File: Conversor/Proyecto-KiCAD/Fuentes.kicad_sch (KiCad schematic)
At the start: 18 parts, among them J1 Barrel_Jack_Switch, J8 VDDA Header, J9 5V Header, P2 SW_SPDT, P3 SW_SPDT, P5 5V Header, P6 Jumper 2, U5 LM7805_TO252, U6 THB3-1211, U7 LP2985-3.3

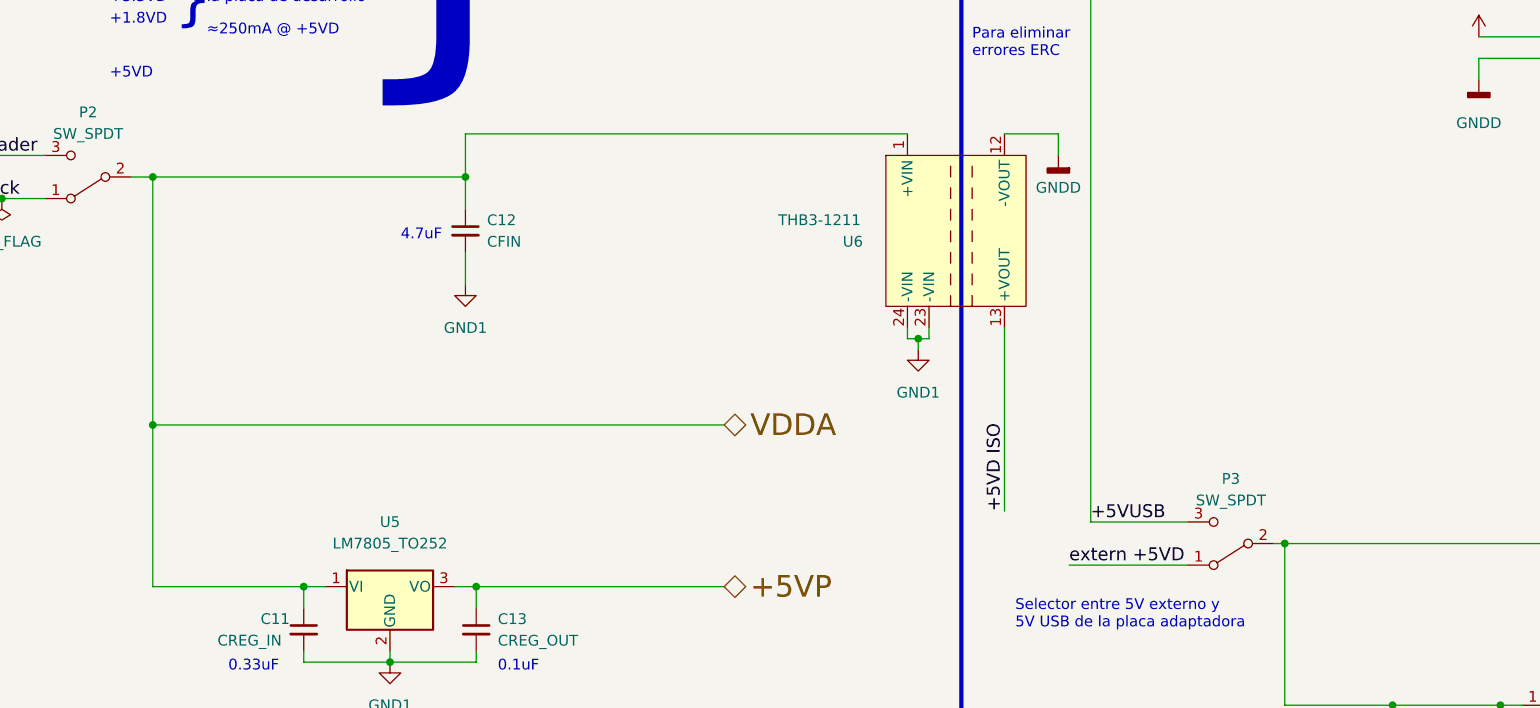
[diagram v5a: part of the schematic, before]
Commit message: Empezar con lar recomendaciones de Jorge
- Agregar nota que contiene todas las recomendaciones (ticks en las que
ya hice)
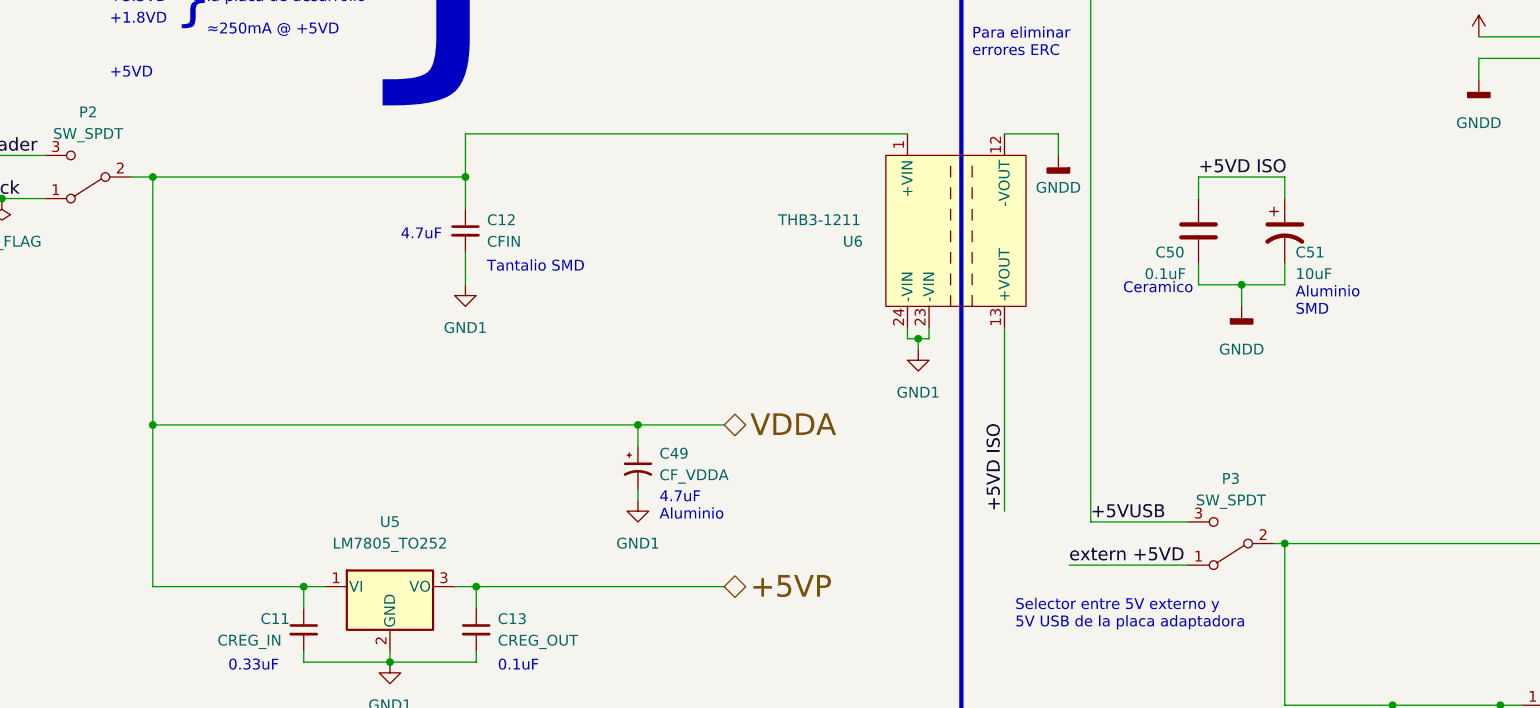
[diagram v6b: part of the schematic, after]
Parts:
- added C49: CF_VDDA, Capacitor_SMD:CP_Elec_3x5.4, symbol Device:C_Polarized_Small_US
- added C50: 0.1uF, Capacitor_SMD:C_1206_3216Metric_Pad1.33x1.80mm_HandSolder, symbol Device:C
- added C51: 10uF, Capacitor_SMD:CP_Elec_3x5.4, symbol Device:C_Polarized_US
- C12: footprint Capacitor_SMD:C_1206_3216Metric_Pad1.33x1.80mm_HandSolder -> Capacitor_Tantalum_SMD:CP_EIA-3528-12_Kemet-T
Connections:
- net +5VD ISO: now also C50.1, C51.1
- net GND1: now also C49.2
- net GNDD: now also C50.2, C51.2
- net VDDA: now also C49.1
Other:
- note added: "4.7uF Aluminio"
- note added: "Aluminio SMD"
- note added: "Ceramico"
- note added: "Tantalio SMD"
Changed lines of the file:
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@@
   (junction (at 31.75 85.09) (diameter 0) (color 0 0 0 0)
   )
+  (junction (at 118.11 106.68) (diameter 0) (color 0 0 0 0)
+  )
   (junction (at 151.13 96.52) (diameter 0) (color 0 0 0 0)
   )
   (junction (at 60.96 77.47) (diameter 0) (color 0 0 0 0)
   )
+  (junction (at 189.23 90.17) (diameter 0) (color 0 0 0 0)
+  )
   (junction (at 261.62 139.7) (diameter 0) (color 0 0 0 0)
   )
@@
     (stroke (width 0) (type default) (color 0 0 0 0))
   )
+  (wire (pts (xy 189.23 92.71) (xy 189.23 90.17))
+    (stroke (width 0) (type default) (color 0 0 0 0))
+  )
   (wire (pts (xy 217.17 63.5) (xy 227.33 63.5))
     (stroke (width 0) (type default) (color 0 0 0 0))
@@
     (stroke (width 0) (type default) (color 0 0 0 0))
   )
+  (wire (pts (xy 194.31 77.47) (xy 194.31 80.01))
+    (stroke (width 0) (type default) (color 0 0 0 0))
+  )
   (wire (pts (xy 138.43 147.32) (xy 152.4 147.32))
     (stroke (width 0) (type default) (color 0 0 0 0))
@@
     (stroke (width 0) (type default) (color 0 0 0 0))
   )
+  (wire (pts (xy 194.31 87.63) (xy 194.31 90.17))
+    (stroke (width 0) (type default) (color 0 0 0 0))
+  )
+  (wire (pts (xy 184.15 77.47) (xy 194.31 77.47))
+    (stroke (width 0) (type default) (color 0 0 0 0))
+  )
+  (wire (pts (xy 184.15 80.01) (xy 184.15 77.47))
+    (stroke (width 0) (type default) (color 0 0 0 0))
+  )
   (wire (pts (xy 207.01 139.7) (xy 207.01 144.78))
     (stroke (width 0) (type default) (color 0 0 0 0))
@@
     (stroke (width 0) (type default) (color 0 0 0 0))
   )
+  (wire (pts (xy 118.11 106.68) (xy 128.27 106.68))
+    (stroke (width 0) (type default) (color 0 0 0 0))
+  )
   (polyline (pts (xy 224.79 48.26) (xy 224.79 17.78))
     (stroke (width 0) (type default) (color 0 0 0 0))
   )
+  (wire (pts (xy 118.11 106.68) (xy 118.11 109.22))
+    (stroke (width 0) (type default) (color 0 0 0 0))
+  )
   (wire (pts (xy 242.57 139.7) (xy 261.62 139.7))
     (stroke (width 0) (type default) (color 0 0 0 0))
@@
     (stroke (width 0) (type default) (color 0 0 0 0))
   )
+  (wire (pts (xy 118.11 114.3) (xy 118.11 115.57))
+    (stroke (width 0) (type default) (color 0 0 0 0))
+  )
+  (wire (pts (xy 184.15 90.17) (xy 184.15 87.63))
+    (stroke (width 0) (type default) (color 0 0 0 0))
+  )
   (wire (pts (xy 60.96 77.47) (xy 60.96 106.68))
     (stroke (width 0) (type default) (color 0 0 0 0))
@@
     (stroke (width 0) (type default) (color 0 0 0 0))
   )
-  (wire (pts (xy 60.96 106.68) (xy 128.27 106.68))
+  (wire (pts (xy 60.96 106.68) (xy 118.11 106.68))
     (stroke (width 0) (type default) (color 0 0 0 0))
   )
@@
     (stroke (width 0) (type default) (color 0 0 0 0))
   )
+  (wire (pts (xy 189.23 90.17) (xy 184.15 90.17))
+    (stroke (width 0) (type default) (color 0 0 0 0))
+  )
   (wire (pts (xy 34.29 180.34) (xy 34.29 177.8))
     (stroke (width 0) (type default) (color 0 0 0 0))
@@
   )
   (wire (pts (xy 60.96 77.47) (xy 97.79 77.47))
+    (stroke (width 0) (type default) (color 0 0 0 0))
+  )
+  (wire (pts (xy 194.31 90.17) (xy 189.23 90.17))
     (stroke (width 0) (type default) (color 0 0 0 0))
   )
@@
     (effects (font (size 2.54 2.54) (thickness 0.508) bold) (justify left bottom))
   )
+  (text "Tantalio SMD" (at 100.33 88.9 0)
+    (effects (font (size 1.27 1.27)) (justify left bottom))
+  )
   (text "Potencia: 7.5mA" (at 19.05 35.56 0)
     (effects (font (size 1.27 1.27)) (justify left bottom))
@@
     (effects (font (size 1.27 1.27)) (justify left bottom))
   )
+  (text "Aluminio\nSMD" (at 195.58 93.98 0)
+    (effects (font (size 1.27 1.27)) (justify left bottom))
+  )
   (text "Potencia" (at 134.62 195.58 0)
     (effects (font (size 2.54 2.54) (thickness 0.508) bold) (justify left bottom))
@@
     (effects (font (size 1.27 1.27)) (justify left bottom))
   )
+  (text "Ceramico" (at 175.26 91.44 0)
+    (effects (font (size 1.27 1.27)) (justify left bottom))
+  )
   (text "-------------" (at 34.29 66.04 0)
     (effects (font (size 1.27 1.27)) (justify left bottom))
@@
     (effects (font (size 1.27 1.27)) (justify left bottom))
   )
+  (text "4.7uF\nAluminio" (at 120.65 118.11 0)
+    (effects (font (size 1.27 1.27)) (justify left bottom))
+  )
   (text "2.2A" (at 121.92 45.72 0)
     (effects (font (size 1.27 1.27)) (justify left bottom))
@@
     (effects (font (size 1.524 1.524)) (justify left bottom))
   )
+  (label "+5VD ISO" (at 184.15 77.47 0)
+    (effects (font (size 1.524 1.524)) (justify left bottom))
+  )
   (label "VDDA Header" (at 33.02 74.93 0)
     (effects (font (size 1.524 1.524)) (justify left bottom))
@@
   (hierarchical_label "+5VD" (shape bidirectional) (at 266.7 120.65 0)
     (effects (font (size 2.54 2.54)) (justify left))
+  )
+  (symbol (lib_id "power:GND1") (at 118.11 115.57 0) (unit 1)
+    (in_bom yes) (on_board yes) (fields_autoplaced)
+    (property "Reference" "#PWR0102" (id 0) (at 118.11 121.92 0)
+      (effects (font (size 1.27 1.27)) hide)
+    )
+    (property "Value" "GND1" (id 1) (at 118.11 120.65 0))
+    (property "Footprint" "" (id 2) (at 118.11 115.57 0)
+      (effects (font (size 1.27 1.27)) hide)
+    )
+    (property "Datasheet" "" (id 3) (at 118.11 115.57 0)
+      (effects (font (size 1.27 1.27)) hide)
+    )
+    (pin "1")
   )
   (symbol (lib_id "power:GNDD") (at 198.12 35.56 0) (unit 1)
@@
     (pin "1")
   )
+  (symbol (lib_id "Device:C") (at 184.15 83.82 0) (unit 1)
+    (in_bom yes) (on_board yes)
+    (property "Reference" "C50" (id 0) (at 179.07 86.36 0)
+      (effects (font (size 1.27 1.27)) (justify left))
+    )
+    (property "Value" "0.1uF" (id 1) (at 177.8 88.9 0)
+      (effects (font (size 1.27 1.27)) (justify left))
+    )
+    (property "Footprint" "Capacitor_SMD:C_1206_3216Metric_Pad1.33x1.80mm_HandSolder" (id 2) (at 185.1152 87.63 0)
+      (effects (font (size 1.27 1.27)) hide)
+    )
+    (property "Datasheet" "~" (id 3) (at 184.15 83.82 0)
+      (effects (font (size 1.27 1.27)) hide)
+    )
+    (pin "1")
+    (pin "2")
+  )
   (symbol (lib_id "power:PWR_FLAG") (at 43.18 80.01 0) (mirror x) (unit 1)
     (in_bom yes) (on_board yes) (fields_autoplaced)
@@
     (pin "2")
   )
+  (symbol (lib_id "power:GNDD") (at 189.23 92.71 0) (unit 1)
+    (in_bom yes) (on_board yes) (fields_autoplaced)
+    (property "Reference" "#PWR0101" (id 0) (at 189.23 99.06 0)
+      (effects (font (size 1.27 1.27)) hide)
+    )
+    (property "Value" "GNDD" (id 1) (at 189.23 97.79 0))
+    (property "Footprint" "" (id 2) (at 189.23 92.71 0)
+      (effects (font (size 1.27 1.27)) hide)
+    )
+    (property "Datasheet" "" (id 3) (at 189.23 92.71 0)
+      (effects (font (size 1.27 1.27)) hide)
+    )
+    (pin "1")
+  )
   (symbol (lib_id "Device:C_Small") (at 97.79 83.82 0) (unit 1)
     (in_bom yes) (on_board yes) (fields_autoplaced)
@@
       (effects (font (size 1.27 1.27)) (justify left))
     )
-    (property "Footprint" "Capacitor_SMD:C_1206_3216Metric_Pad1.33x1.80mm_HandSolder" (id 2) (at 97.79 83.82 0)
+    (property "Footprint" "Capacitor_Tantalum_SMD:CP_EIA-3528-12_Kemet-T" (id 2) (at 97.79 83.82 0)
       (effects (font (size 1.27 1.27)) hide)
     )
@@
     (pin "1")
   )
+  (symbol (lib_id "Device:C_Polarized_US") (at 194.31 83.82 0) (unit 1)
+    (in_bom yes) (on_board yes)
+    (property "Reference" "C51" (id 0) (at 195.58 86.36 0)
+      (effects (font (size 1.27 1.27)) (justify left))
+    )
+    (property "Value" "10uF" (id 1) (at 195.58 88.9 0)
+      (effects (font (size 1.27 1.27)) (justify left))
+    )
+    (property "Footprint" "Capacitor_SMD:CP_Elec_3x5.4" (id 2) (at 194.31 83.82 0)
+      (effects (font (size 1.27 1.27)) hide)
+    )
+    (property "Datasheet" "~" (id 3) (at 194.31 83.82 0)
+      (effects (font (size 1.27 1.27)) hide)
+    )
+    (pin "1")
+    (pin "2")
+  )
   (symbol (lib_id "Switch:SW_SPDT") (at 187.96 120.65 180) (unit 1)
     (in_bom yes) (on_board yes) (fields_autoplaced)
@@
     (pin "1")
   )
+  (symbol (lib_id "Device:C_Polarized_Small_US") (at 118.11 111.76 0) (unit 1)
+    (in_bom yes) (on_board yes) (fields_autoplaced)
+    (property "Reference" "C49" (id 0) (at 120.65 110.0581 0)
+      (effects (font (size 1.27 1.27)) (justify left))
+    )
+    (property "Value" "CF_VDDA" (id 1) (at 120.65 112.5981 0)
+      (effects (font (size 1.27 1.27)) (justify left))
+    )
+    (property "Footprint" "Capacitor_SMD:CP_Elec_3x5.4" (id 2) (at 118.11 111.76 0)
+      (effects (font (size 1.27 1.27)) hide)
+    )
+    (property "Datasheet" "~" (id 3) (at 118.11 111.76 0)
+      (effects (font (size 1.27 1.27)) hide)
+    )
+    (pin "1")
+    (pin "2")
+  )
   (symbol (lib_id "Device:R_US") (at 156.21 152.4 90) (unit 1)

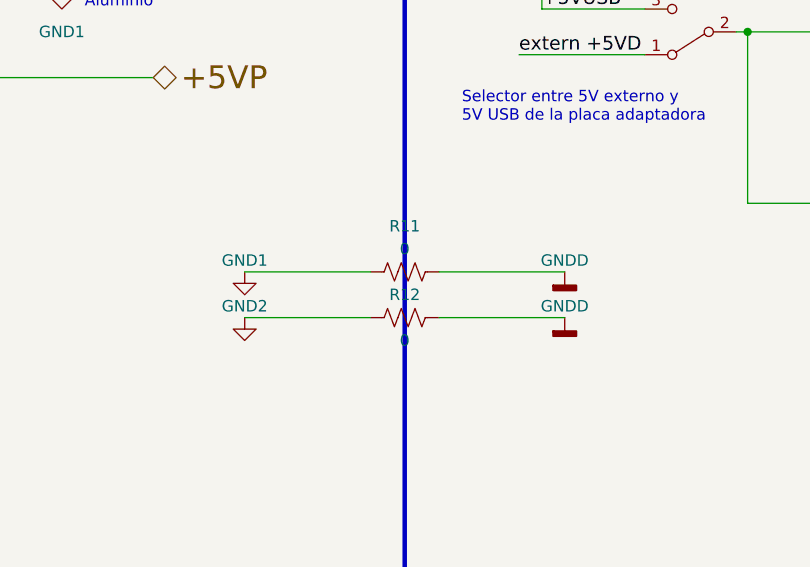
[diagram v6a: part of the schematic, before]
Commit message: Corregir las cosas que me indico Jorge
- Por hacer:
  - Verificar las correcciones con Jorge
  - Ver si se consigue un capacitor mas chico (~20mm) para la entrada
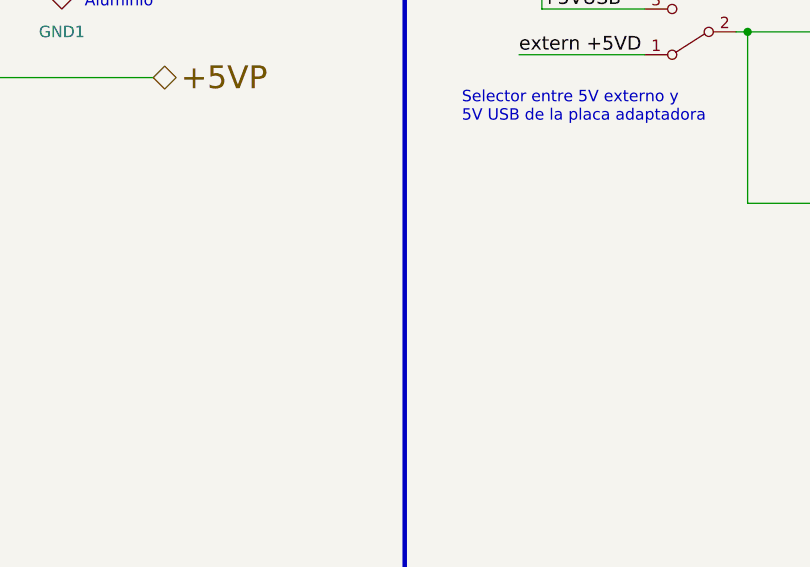
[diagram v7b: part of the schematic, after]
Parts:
- removed R11, R12: 0, Resistor_SMD:R_1206_3216Metric_Pad1.30x1.75mm_HandSolder, symbol Device:R_US
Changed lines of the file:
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@@
-    (stroke (width 0) (type default) (color 0 0 0 0))
-  )
-  (wire (pts (xy 138.43 147.32) (xy 152.4 147.32))
     (stroke (width 0) (type default) (color 0 0 0 0))
   )
@@
     (stroke (width 0) (type default) (color 0 0 0 0))
   )
-  (wire (pts (xy 138.43 152.4) (xy 152.4 152.4))
-    (stroke (width 0) (type default) (color 0 0 0 0))
-  )
   (wire (pts (xy 78.74 125.73) (xy 78.74 128.27))
     (stroke (width 0) (type default) (color 0 0 0 0))
@@
   )
   (polyline (pts (xy 63.5 162.56) (xy 16.51 162.56))
-    (stroke (width 0) (type default) (color 0 0 0 0))
-  )
-  (wire (pts (xy 160.02 147.32) (xy 173.99 147.32))
     (stroke (width 0) (type default) (color 0 0 0 0))
   )
@@
   )
   (wire (pts (xy 34.29 180.34) (xy 34.29 177.8))
-    (stroke (width 0) (type default) (color 0 0 0 0))
-  )
-  (wire (pts (xy 160.02 152.4) (xy 173.99 152.4))
     (stroke (width 0) (type default) (color 0 0 0 0))
   )
@@
     (pin "1")
   )
-  (symbol (lib_id "Device:R_US") (at 156.21 147.32 90) (unit 1)
-    (in_bom yes) (on_board yes)
-    (property "Reference" "R11" (id 0) (at 156.21 142.24 90))
-    (property "Value" "0" (id 1) (at 156.21 144.78 90))
-    (property "Footprint" "Resistor_SMD:R_1206_3216Metric_Pad1.30x1.75mm_HandSolder" (id 2) (at 156.464 146.304 90)
-      (effects (font (size 1.27 1.27)) hide)
-    )
-    (property "Datasheet" "~" (id 3) (at 156.21 147.32 0)
-      (effects (font (size 1.27 1.27)) hide)
-    )
-    (pin "1")
-    (pin "2")
-  )
-  (symbol (lib_id "power:GNDD") (at 173.99 147.32 0) (unit 1)
-    (in_bom yes) (on_board yes)
-    (property "Reference" "#PWR036" (id 0) (at 173.99 153.67 0)
-      (effects (font (size 1.27 1.27)) hide)
-    )
-    (property "Value" "GNDD" (id 1) (at 173.99 146.05 0))
-    (property "Footprint" "" (id 2) (at 173.99 147.32 0)
-      (effects (font (size 1.27 1.27)) hide)
-    )
-    (property "Datasheet" "" (id 3) (at 173.99 147.32 0)
-      (effects (font (size 1.27 1.27)) hide)
-    )
-    (pin "1")
-  )
-  (symbol (lib_id "power:GND1") (at 138.43 147.32 0) (unit 1)
-    (in_bom yes) (on_board yes)
-    (property "Reference" "#PWR032" (id 0) (at 138.43 153.67 0)
-      (effects (font (size 1.27 1.27)) hide)
-    )
-    (property "Value" "GND1" (id 1) (at 138.43 146.05 0))
-    (property "Footprint" "" (id 2) (at 138.43 147.32 0)
-      (effects (font (size 1.27 1.27)) hide)
-    )
-    (property "Datasheet" "" (id 3) (at 138.43 147.32 0)
-      (effects (font (size 1.27 1.27)) hide)
-    )
-    (pin "1")
-  )
   (symbol (lib_id "Device:C_Polarized_US") (at 194.31 83.82 0) (unit 1)
     (in_bom yes) (on_board yes)
@@
     (pin "2")
     (pin "3")
-  )
-  (symbol (lib_id "power:GNDD") (at 173.99 152.4 0) (unit 1)
-    (in_bom yes) (on_board yes)
-    (property "Reference" "#PWR037" (id 0) (at 173.99 158.75 0)
-      (effects (font (size 1.27 1.27)) hide)
-    )
-    (property "Value" "GNDD" (id 1) (at 173.99 151.13 0))
-    (property "Footprint" "" (id 2) (at 173.99 152.4 0)
-      (effects (font (size 1.27 1.27)) hide)
-    )
-    (property "Datasheet" "" (id 3) (at 173.99 152.4 0)
-      (effects (font (size 1.27 1.27)) hide)
-    )
-    (pin "1")
   )
   (symbol (lib_id "power:GND1") (at 35.56 88.9 0) (unit 1)
@@
     (pin "2")
   )
-  (symbol (lib_id "Device:R_US") (at 156.21 152.4 90) (unit 1)
-    (in_bom yes) (on_board yes)
-    (property "Reference" "R12" (id 0) (at 156.21 149.86 90))
-    (property "Value" "0" (id 1) (at 156.21 154.94 90))
-    (property "Footprint" "Resistor_SMD:R_1206_3216Metric_Pad1.30x1.75mm_HandSolder" (id 2) (at 156.464 151.384 90)
-      (effects (font (size 1.27 1.27)) hide)
-    )
-    (property "Datasheet" "~" (id 3) (at 156.21 152.4 0)
-      (effects (font (size 1.27 1.27)) hide)
-    )
-    (pin "1")
-    (pin "2")
-  )
   (symbol (lib_id "Regulator_Linear:LP2985-3.3") (at 232.41 142.24 0) (unit 1)
     (in_bom yes) (on_board yes) (fields_autoplaced)
@@
     (pin "5")
   )
-  (symbol (lib_id "power:GND2") (at 138.43 152.4 0) (unit 1)
-    (in_bom yes) (on_board yes)
-    (property "Reference" "#PWR033" (id 0) (at 138.43 158.75 0)
-      (effects (font (size 1.27 1.27)) hide)
-    )
-    (property "Value" "GND2" (id 1) (at 138.43 151.13 0))
-    (property "Footprint" "" (id 2) (at 138.43 152.4 0)
-      (effects (font (size 1.27 1.27)) hide)
-    )
-    (property "Datasheet" "" (id 3) (at 138.43 152.4 0)
-      (effects (font (size 1.27 1.27)) hide)
-    )
-    (pin "1")
-  )
   (symbol (lib_id "power:GND1") (at 88.9 134.62 0) (unit 1)
